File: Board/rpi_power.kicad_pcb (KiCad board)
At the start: 2 copper layers, 69 x 57.4 mm, 68 parts, among them J1 POWER, J2 Raspberry_Pi_2_3, J3 Raspberry_Pi_2_3, J4 ADC, J7 PROG, J9 GPIO, Q10 IRLML6344TRPBF, Q6 IRLML6344TRPBF, U1 TPS54625, U2 ATxmega16A4U-AU, U3 LM2936-3.3, Y1 Crystal

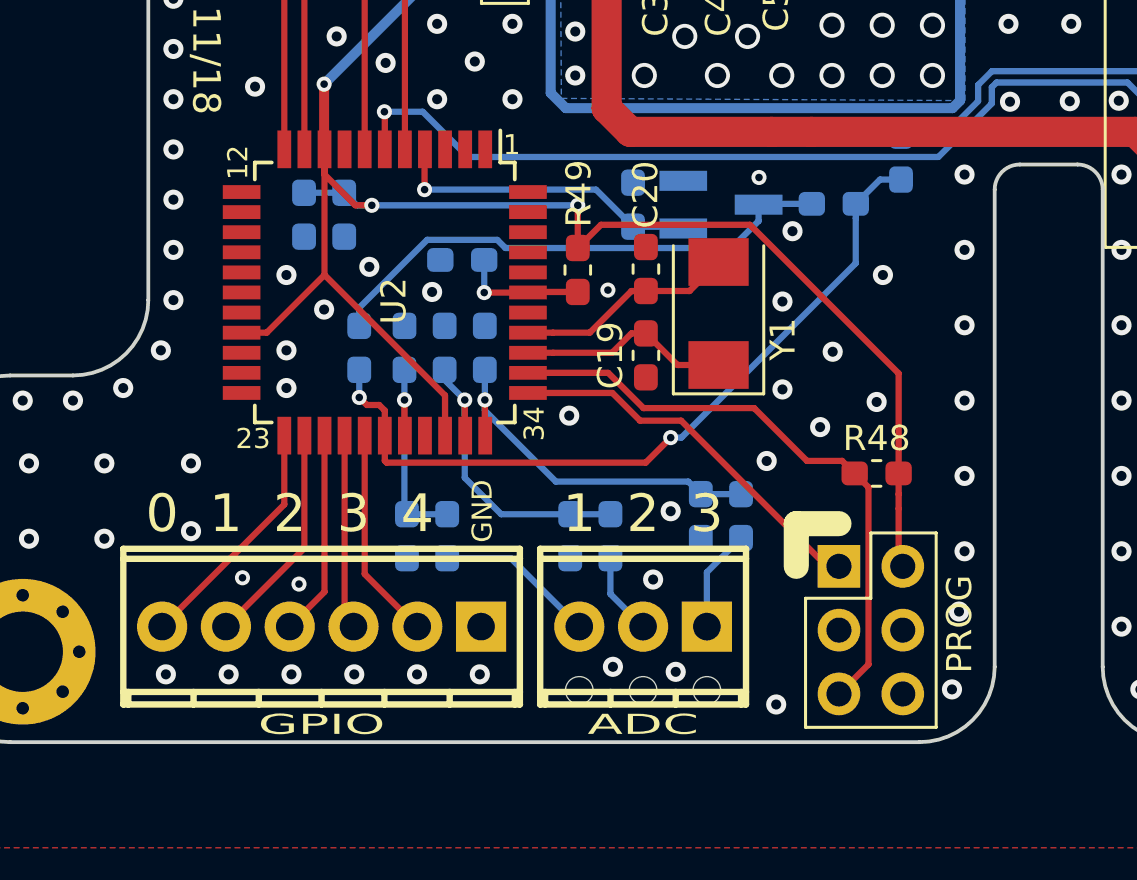
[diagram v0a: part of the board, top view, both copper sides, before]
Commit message: Added protection resistors on xmega GPIOs. Corrected prog connector outline.
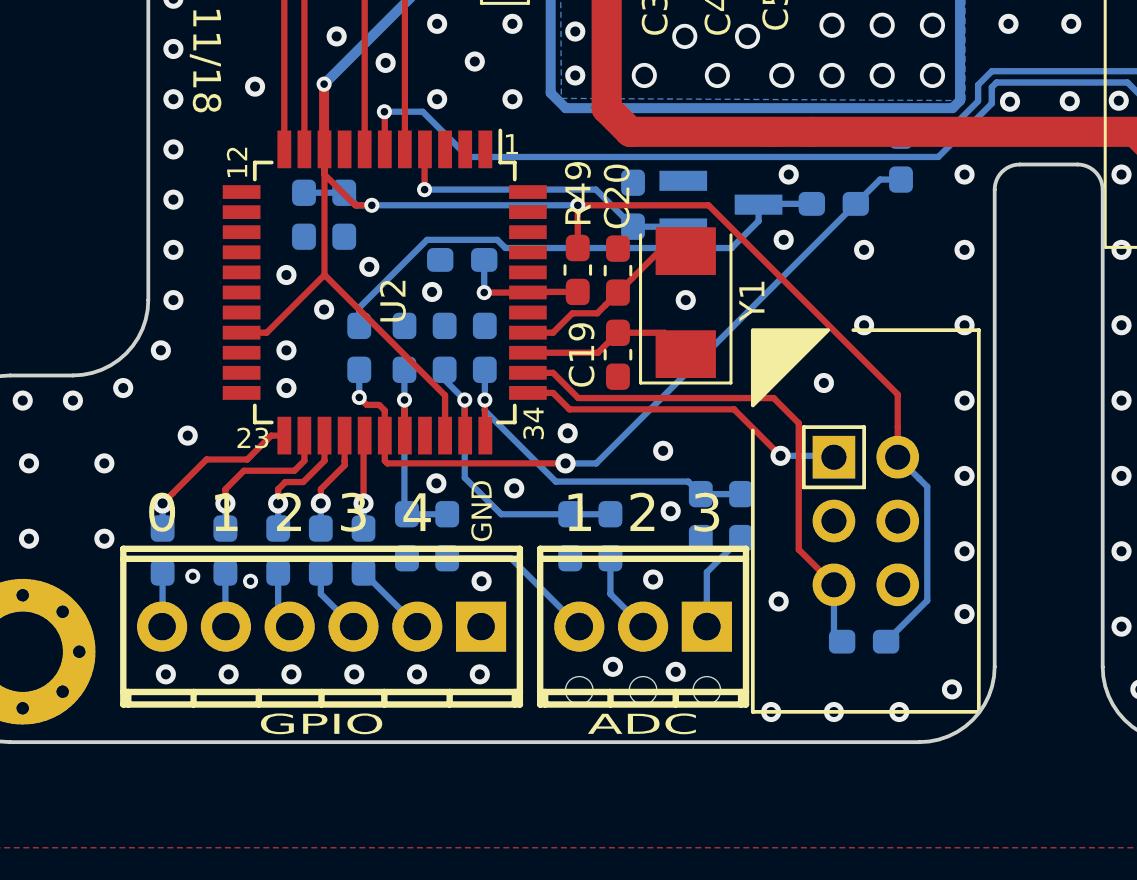
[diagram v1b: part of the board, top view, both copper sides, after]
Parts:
- added R14: 10, Resistor_SMD:R_0603_1608Metric_Pad1.05x0.95mm_HandSolder, B.Cu at (125.6, 116.0)
- added R15: 10, Resistor_SMD:R_0603_1608Metric_Pad1.05x0.95mm_HandSolder, B.Cu at (128.1, 116.0)
- added R16: 10, Resistor_SMD:R_0603_1608Metric_Pad1.05x0.95mm_HandSolder, B.Cu at (130.2, 116.0)
- added R17: 10, Resistor_SMD:R_0603_1608Metric_Pad1.05x0.95mm_HandSolder, B.Cu at (131.9, 116.0)
- added R18: 10, Resistor_SMD:R_0603_1608Metric_Pad1.05x0.95mm_HandSolder, B.Cu at (133.6, 116.0)
- J7: footprint Connector_PinHeader_2.54mm:PinHeader_2x03_P2.54mm_Vertical -> Connectors_custom:PinHeader_2x03_P2.54mm_Vertical_w_enclosure
- R43, R45: value 1k -> 4.7k
- R47: value 4.7k -> 10k
- R48: moved to B.Cu
- R7: value 22.1k 1% -> 22.1k
- moved R48 6.72 mm to (153.5, 119.6)
- moved J7 2.10 mm to (153.6, 114.8)
- moved Y1 1.37 mm to (146.4, 106.1)
- moved C20 1.11 mm to (143.7, 104.8)
- moved C19 1.11 mm to (143.7, 108.2)
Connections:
- U2 pad 23: GPIO0 -> Net-(R14-Pad1)
- U2 pad 24: GPIO1 -> Net-(R15-Pad1)
- U2 pad 25: GPIO2 -> Net-(R16-Pad1)
- U2 pad 26: GPIO3 -> Net-(R17-Pad1)
- U2 pad 27: GPIO4 -> Net-(R18-Pad1)
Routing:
- net GPIO0: track 9.62 -> 2.16 mm
- net Net-(R14-Pad1): track 0.00 -> 6.96 mm, vias 0 -> 1
- net GPIO1: track 8.90 -> 2.16 mm
- net Net-(R15-Pad1): track 0.00 -> 6.18 mm, vias 0 -> 1
- net GPIO2: track 8.18 -> 2.35 mm
- net GPIO4: track 8.47 -> 3.04 mm
- net Net-(R16-Pad1): track 0.00 -> 4.88 mm, vias 0 -> 1
- net GPIO3: track 8.25 -> 3.69 mm
- net Net-(R17-Pad1): track 0.00 -> 4.09 mm, vias 0 -> 1
- net Net-(R18-Pad1): track 0.00 -> 3.72 mm, vias 0 -> 1
- net VCC: track 71.6 -> 75.1 mm
- net PDI_CLK: track 24.2 -> 21.0 mm
- net PDI_DATA: track 15.2 -> 13.2 mm, vias 0 -> 1
- net Net-(C19-Pad1): track 8.43 -> 6.97 mm
- net ADC0: track 31.0 -> 29.6 mm
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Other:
- board text added: "RPi_power Rev. B"
- board text removed: "RPi_power Rev. A"

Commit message: Some corrections.
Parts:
- removed G***: LOGO, Logos:taz
- R32: value 51k -> 22.1k
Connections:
- J7 pad 3: (no net) -> Net-(J7-Pad3)
- J7 pad 4: (no net) -> Net-(J7-Pad4)
- U2 pad 1: (no net) -> Net-(U2-Pad1)
- U2 pad 12: (no net) -> Net-(U2-Pad12)
- U2 pad 13: (no net) -> Net-(U2-Pad13)
- U2 pad 14: (no net) -> Net-(U2-Pad14)
- U2 pad 15: (no net) -> Net-(U2-Pad15)
- U2 pad 16: (no net) -> Net-(U2-Pad16)
- U2 pad 17: (no net) -> Net-(U2-Pad17)
- U2 pad 2: (no net) -> Net-(U2-Pad2)
- U2 pad 20: (no net) -> Net-(U2-Pad20)
- U2 pad 21: (no net) -> Net-(U2-Pad21)
- U2 pad 22: (no net) -> Net-(U2-Pad22)
- U2 pad 3: (no net) -> Net-(U2-Pad3)
- U2 pad 40: (no net) -> Net-(U2-Pad40)
- U2 pad 41: (no net) -> Net-(U2-Pad41)
- U2 pad 42: (no net) -> Net-(U2-Pad42)
- U2 pad 43: (no net) -> Net-(U2-Pad43)
- U2 pad 44: (no net) -> Net-(U2-Pad44)

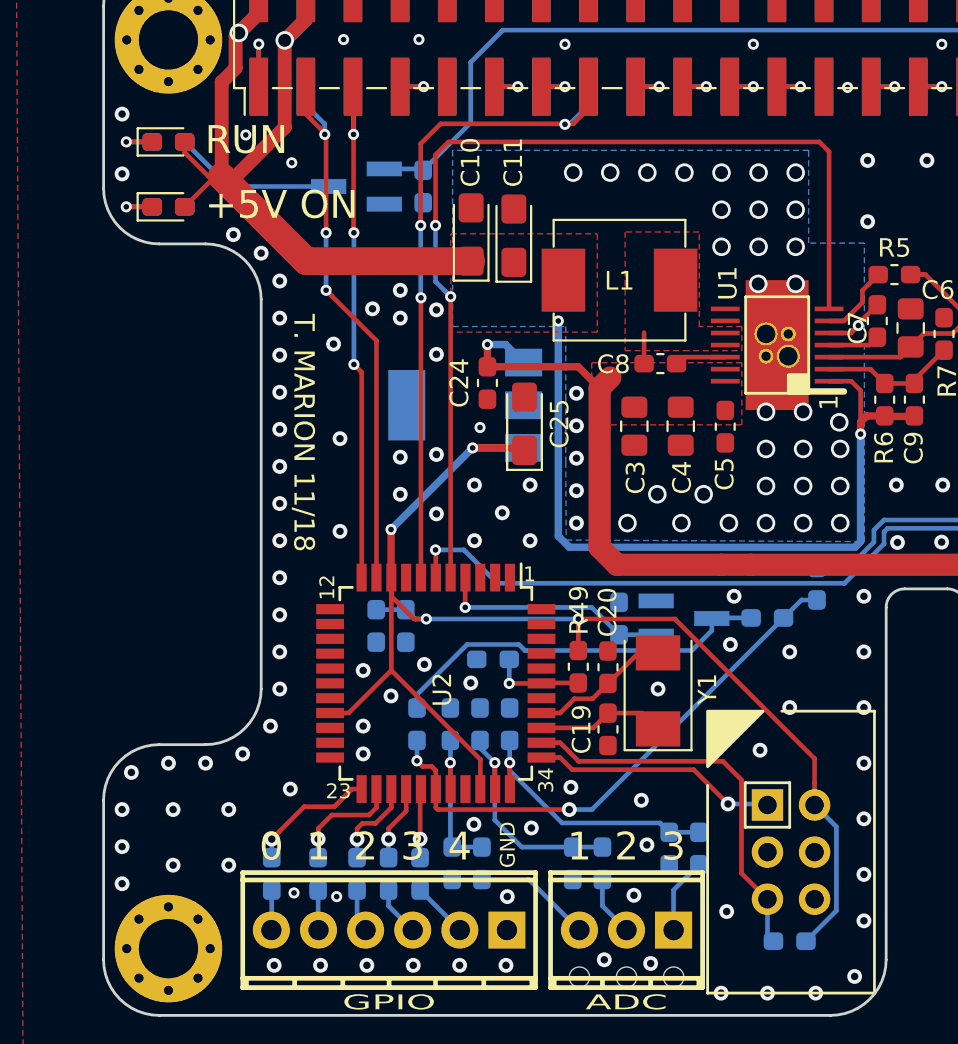
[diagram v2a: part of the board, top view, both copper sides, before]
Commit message: MAJOR CORRECTION: moved ADCs to correct port on xmega. Added a LED controlled by the xmega.
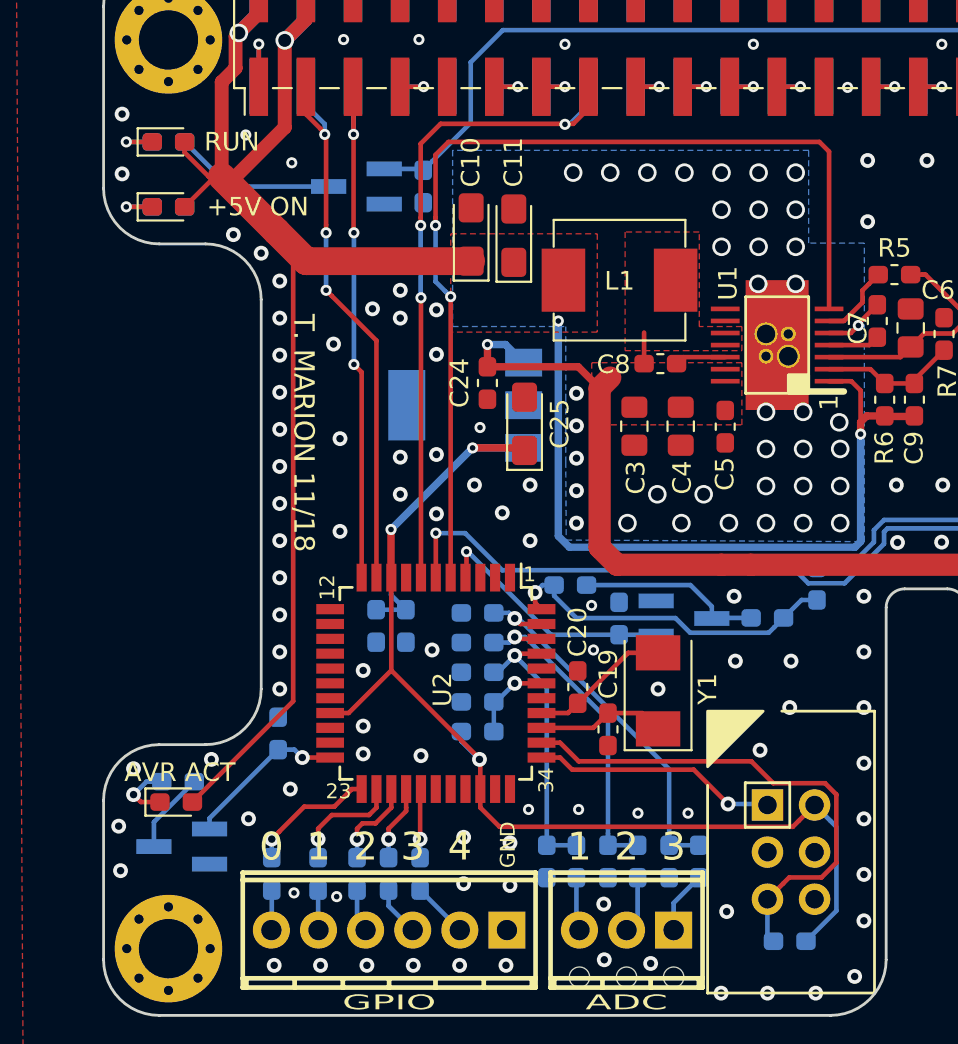
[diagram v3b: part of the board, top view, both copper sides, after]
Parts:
- added D4: LED_BLUE, LED_SMD:LED_0603_1608Metric_Pad1.05x0.95mm_HandSolder, F.Cu at (120.4, 112.1)
- added Q1: IRLML6344TRPBF, Package_TO_SOT_SMD:SOT-23_Handsoldering, B.Cu at (120.7, 114.5)
- added R19: 10k, Resistor_SMD:R_0603_1608Metric_Pad1.05x0.95mm_HandSolder, B.Cu at (125.9, 108.4)
- added R20: 4.7k, Resistor_SMD:R_0603_1608Metric_Pad1.05x0.95mm_HandSolder, B.Cu at (120.5, 111.0)
- R49: moved to B.Cu
- moved C15 11.2 mm to (141.7, 100.4), turned to 0 degrees
- moved R49 6.46 mm to (136.7, 108.3), turned to 0 degrees
- moved C14 6.25 mm to (136.7, 101.9), turned to 180 degrees
- moved R8 5.10 mm to (142.0, 115.3)
- moved R9 5.10 mm to (140.4, 115.3)
- moved C13 4.41 mm to (136.7, 103.5), turned to 180 degrees
- moved C12 3.17 mm to (136.7, 105.1), turned to 180 degrees
- moved C23 2.44 mm to (136.7, 106.7)
- moved C20 1.95 mm to (142.1, 105.9)
- moved R10 1.90 mm to (145.3, 115.3)
- moved R11 1.90 mm to (143.7, 115.3)
- moved R12 0.70 mm to (148.6, 115.3)
- moved R13 0.70 mm to (147.0, 115.3)
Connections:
- C15 pad 1: ADC0 -> ADC4
- J7 pad 3: Net-(J7-Pad3) -> (no net)
- J7 pad 4: Net-(J7-Pad4) -> (no net)
- R31 pad 2: ADC0 -> ADC4
- R32 pad 1: ADC0 -> ADC4
- U2 pad 1: Net-(U2-Pad1) -> (no net)
- U2 pad 12: Net-(U2-Pad12) -> (no net)
- U2 pad 13: Net-(U2-Pad13) -> (no net)
- U2 pad 14: Net-(U2-Pad14) -> (no net)
- U2 pad 15: Net-(U2-Pad15) -> (no net)
- U2 pad 16: Net-(U2-Pad16) -> (no net)
- U2 pad 17: Net-(U2-Pad17) -> (no net)
- U2 pad 2: Net-(U2-Pad2) -> (no net)
- U2 pad 20: Net-(U2-Pad20) -> (no net)
- U2 pad 21: Net-(U2-Pad21) -> (no net)
- U2 pad 22: Net-(U2-Pad22) -> LED_AVR
- U2 pad 28: ADC0 -> (no net)
- U2 pad 29: ADC1 -> (no net)
- U2 pad 3: Net-(U2-Pad3) -> (no net)
- U2 pad 32: ADC2 -> (no net)
- U2 pad 33: ADC3 -> (no net)
- U2 pad 40: Net-(U2-Pad40) -> (no net)
- U2 pad 41: Net-(U2-Pad41) -> ADC1
- U2 pad 42: Net-(U2-Pad42) -> ADC2
- U2 pad 43: Net-(U2-Pad43) -> ADC3
- U2 pad 44: Net-(U2-Pad44) -> ADC4
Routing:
- net +5V: track 91.7 -> 125.1 mm
- net ADC0: track 29.6 -> 0.00 mm, vias 2 -> 0
- net ADC4: track 0.00 -> 18.5 mm, vias 0 -> 1
- net Net-(C15-Pad2): track 21.1 -> 10.0 mm
- net LED_AVR: track 0.00 -> 8.78 mm, vias 0 -> 1
- net ADC1: track 8.82 -> 15.5 mm
- net PDI_CLK: track 21.0 -> 27.7 mm
- net VCC: track 75.1 -> 68.7 mm, vias 4 -> 3
- net ADC3: track 14.6 -> 20.2 mm
- net ADC2: track 12.5 -> 18.0 mm
- net Net-(Q1-Pad3): track 0.00 -> 4.40 mm
- net ADC1_IN: track 6.39 -> 2.89 mm
- net Net-(D4-Pad1): track 0.00 -> 3.41 mm, vias 0 -> 1
- net POWER_STATE: track 92.1 -> 93.3 mm
- net BATT+_MEASURE: track 12.7 -> 13.6 mm
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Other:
- board text added: "AVR ACT"
